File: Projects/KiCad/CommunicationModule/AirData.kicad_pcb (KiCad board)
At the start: 2 copper layers, 110 x 95 mm, 26 parts, among them J1 Conn_01x04_Pin, J2 Conn_01x04_Pin, J3 Micro_SD_Card_Det_Hirose_DM3AT, U1 ABX00012, U2 MCP2562-E-P, U3 LT1584-3.3, U4 TLP222A, U5 MCP2515-I/P, Y1 8MHz

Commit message: ミッションモジュール, エアデータ通信モジュール, システムデータ通信モジュールのKiCadを追加
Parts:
- removed C3, C4: 0.1μF, Capacitor_SMD:C_0805_2012Metric_Pad1.18x1.45mm_HandSolder
- removed D1: 1N4148, Diode_THT:D_DO-35_SOD27_P7.62mm_Horizontal
- removed F1: Polyfuse, Fuse:Fuse_BelFuse_0ZRE0005FF_L8.3mm_W3.8mm
- removed J3: Micro_SD_Card_Det_Hirose_DM3AT, Connector_Card:microSD_HC_Hirose_DM3AT-SF-PEJM5
- removed R3, R4: 120Ω, Resistor_SMD:R_0805_2012Metric_Pad1.20x1.40mm_HandSolder
- removed U3: LT1584-3.3, Package_TO_SOT_THT:TO-220-3_Vertical
- removed U4: TLP222A, Package_DIP:DIP-4_W7.62mm
- removed U6: ~, StrawberryLinux_ADXL375_Module:ADXL375
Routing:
- net +3.3V: track 159.2 -> 79.2 mm, vias 4 -> 2
- net I2C_SDA: track 57.8 -> 0.00 mm
- net I2C_SCL: track 55.3 -> 0.00 mm
- net SPI_MISO: track 75.9 -> 27.6 mm
- net SPI_SCLK: track 65.8 -> 21.2 mm
- net +5V: track 106.8 -> 65.6 mm, vias 3 -> 1
- net SPI_MOSI: track 61.8 -> 21.2 mm
- net Net-(D1-A): track 36.2 -> 0.00 mm, vias 1 -> 0
- net MEMORY_POWER_CONTROL: track 36.1 -> 0.00 mm, vias 1 -> 0
- net SPI_CS_SD: track 34.2 -> 0.00 mm
- net MEMORY_POWER: track 19.9 -> 0.00 mm
- net Net-(R3-Pad2): track 9.35 -> 0.00 mm
- net Net-(F1-Pad2): track 7.06 -> 0.00 mm

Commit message: 全モジュールのkicadを一通り作った
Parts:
- added D1: LED, LED_SMD:LED_1206_3216Metric_Pad1.42x1.75mm_HandSolder, F.Cu at (187.0, 73.5)
- added D2: LED, LED_SMD:LED_1206_3216Metric_Pad1.42x1.75mm_HandSolder, F.Cu at (195.5, 109.5)
- added D3: LED, LED_SMD:LED_1206_3216Metric_Pad1.42x1.75mm_HandSolder, F.Cu at (195.5, 114.5)
- added D4: LED, LED_SMD:LED_1206_3216Metric_Pad1.42x1.75mm_HandSolder, F.Cu at (158.5, 134.5)
- added D5: LED, LED_SMD:LED_1206_3216Metric_Pad1.42x1.75mm_HandSolder, F.Cu at (151.5, 134.5)
- added R2: 10kΩ, Resistor_SMD:R_0805_2012Metric_Pad1.20x1.40mm_HandSolder, F.Cu at (172.5, 119.0)
- added R3: 2kΩ, Resistor_SMD:R_0805_2012Metric_Pad1.20x1.40mm_HandSolder, F.Cu at (187.0, 77.0)
- added R4: 100Ω, Resistor_SMD:R_0805_2012Metric_Pad1.20x1.40mm_HandSolder, F.Cu at (190.5, 109.5)
- added R5: 100Ω, Resistor_SMD:R_0805_2012Metric_Pad1.20x1.40mm_HandSolder, F.Cu at (190.5, 114.5)
- added R6: 100Ω, Resistor_SMD:R_0805_2012Metric_Pad1.20x1.40mm_HandSolder, F.Cu at (158.5, 129.0)
- added R7: 100Ω, Resistor_SMD:R_0805_2012Metric_Pad1.20x1.40mm_HandSolder, F.Cu at (151.5, 129.0)
- added SW1: SW_Push, Button_Switch_THT:SW_PUSH_6mm, F.Cu at (141.8, 133.8)
- moved C3 0.71 mm to (172.5, 121.5), turned to 180 degrees
- renumbered C5 to C3, C6 to C4, C7 to C5, U5 to U3
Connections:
- U1 pad 10: unconnected-(U1-PA23_TC4-W1/1-Pad10) -> CAN_RECEIVE_STATUS
- U1 pad 11: unconnected-(U1-PA10_TCC0-W2/~2-Pad11) -> CAN_SEND_STATUS
- U1 pad 12: unconnected-(U1-PA11_TCC0-W3/~3-Pad12) -> LORA_RECEIVE_STATUS
- U1 pad 13: unconnected-(U1-PB10_TCC0-W4/~4-Pad13) -> LORA_SEND_STATUS
- U1 pad 14: MEMORY_POWER_CONTROL -> unconnected-(U1-PB11_TCC0-W5/~5-Pad14)
- U1 pad 15: SPI_CS_SD -> unconnected-(U1-PA20_TCC0-W6-Pad15)
- U1 pad 20: I2C_SDA -> unconnected-(U1-PA08_S0_I2C_SDA-Pad20)
- U1 pad 21: I2C_SCL -> unconnected-(U1-PA09_S0_I2C_SCL-Pad21)
- U1 pad 9: unconnected-(U1-PA22_TC4-W0/0-Pad9) -> DEBUG_MODE
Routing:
- net CAN_RECEIVE_STATUS: track 0.00 -> 76.9 mm
- net CAN_SEND_STATUS: track 0.00 -> 72.0 mm
- net DEBUG_MODE: track 0.00 -> 42.7 mm
- net LORA_RECEIVE_STATUS: track 0.00 -> 33.4 mm
- net LORA_SEND_STATUS: track 0.00 -> 28.9 mm
- net +5V: track 65.6 -> 70.1 mm
- net Net-(D1-A): track 0.00 -> 3.70 mm
- net Net-(U3-~RESET): track 0.00 -> 3.23 mm
- net Net-(D5-A): track 0.00 -> 3.01 mm
- net Net-(D4-A): track 0.00 -> 3.01 mm
- net Net-(D3-A): track 0.00 -> 2.51 mm
- net Net-(D2-A): track 0.00 -> 2.51 mm
- net CAN_TX: track 45.2 -> 46.1 mm
- net +3.3V: track 79.2 -> 79.7 mm
- net GND: vias 0 -> 58
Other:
- board text added: "Boot Selection"
- board text added: "CAN"
- board text added: "CAN-BUS TERMINATION RESISTOR (OPTIONAL)"
- board text added: "DEBUG"
- board text added: "LORA"
- board text added: "POWER"
- board text added: "RECEIVE"
- board text added: "SEND"

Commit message: 一通り部品を選定
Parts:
- C4, C5: footprint Capacitor_SMD:C_0805_2012Metric_Pad1.18x1.45mm_HandSolder -> Capacitor_SMD:C_0603_1608Metric_Pad1.08x0.95mm_HandSolder
- D1: value LED -> RED; footprint LED_SMD:LED_1206_3216Metric_Pad1.42x1.75mm_HandSolder -> LED_SMD:LED_0603_1608Metric_Pad1.05x0.95mm_HandSolder
- D2, D3, D4, D5: value LED -> ORANGE; footprint LED_SMD:LED_1206_3216Metric_Pad1.42x1.75mm_HandSolder -> LED_SMD:LED_0603_1608Metric_Pad1.05x0.95mm_HandSolder
- R1: value 120R1/4W -> 120Ω; footprint Resistor_SMD:R_0805_2012Metric_Pad1.20x1.40mm_HandSolder -> Resistor_SMD:R_0603_1608Metric_Pad0.98x0.95mm_HandSolder
- R2, R4, R5, R6, R7: footprint Resistor_SMD:R_0805_2012Metric_Pad1.20x1.40mm_HandSolder -> Resistor_SMD:R_0603_1608Metric_Pad0.98x0.95mm_HandSolder
- R3: value 2kΩ -> 620Ω; footprint Resistor_SMD:R_0805_2012Metric_Pad1.20x1.40mm_HandSolder -> Resistor_SMD:R_0603_1608Metric_Pad0.98x0.95mm_HandSolder
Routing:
- net Net-(D5-A): track 3.01 -> 3.62 mm
- net Net-(D4-A): track 3.01 -> 3.62 mm
- net Net-(D3-A): track 2.51 -> 3.12 mm
- net Net-(D2-A): track 2.51 -> 3.12 mm

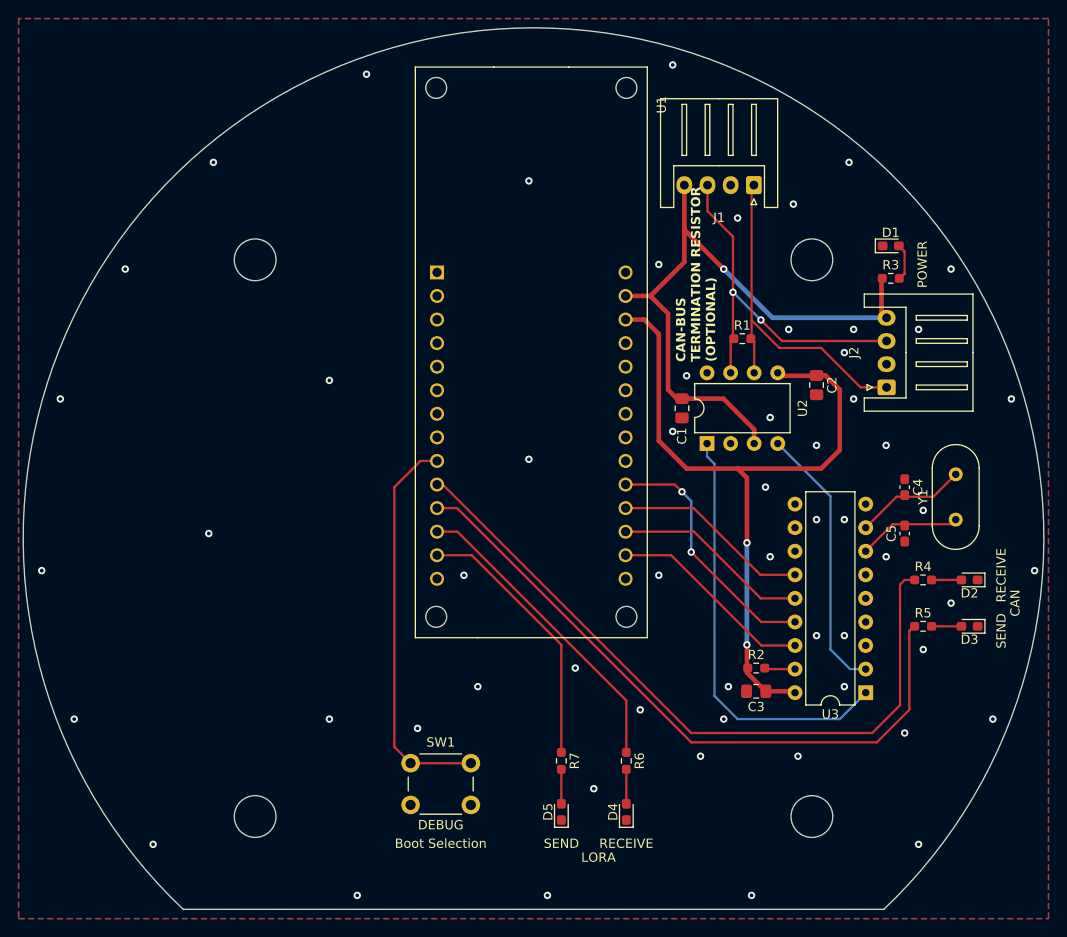
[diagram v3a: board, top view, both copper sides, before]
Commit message: コネクタを再配置, 基板上で12V->5Vをするように変更
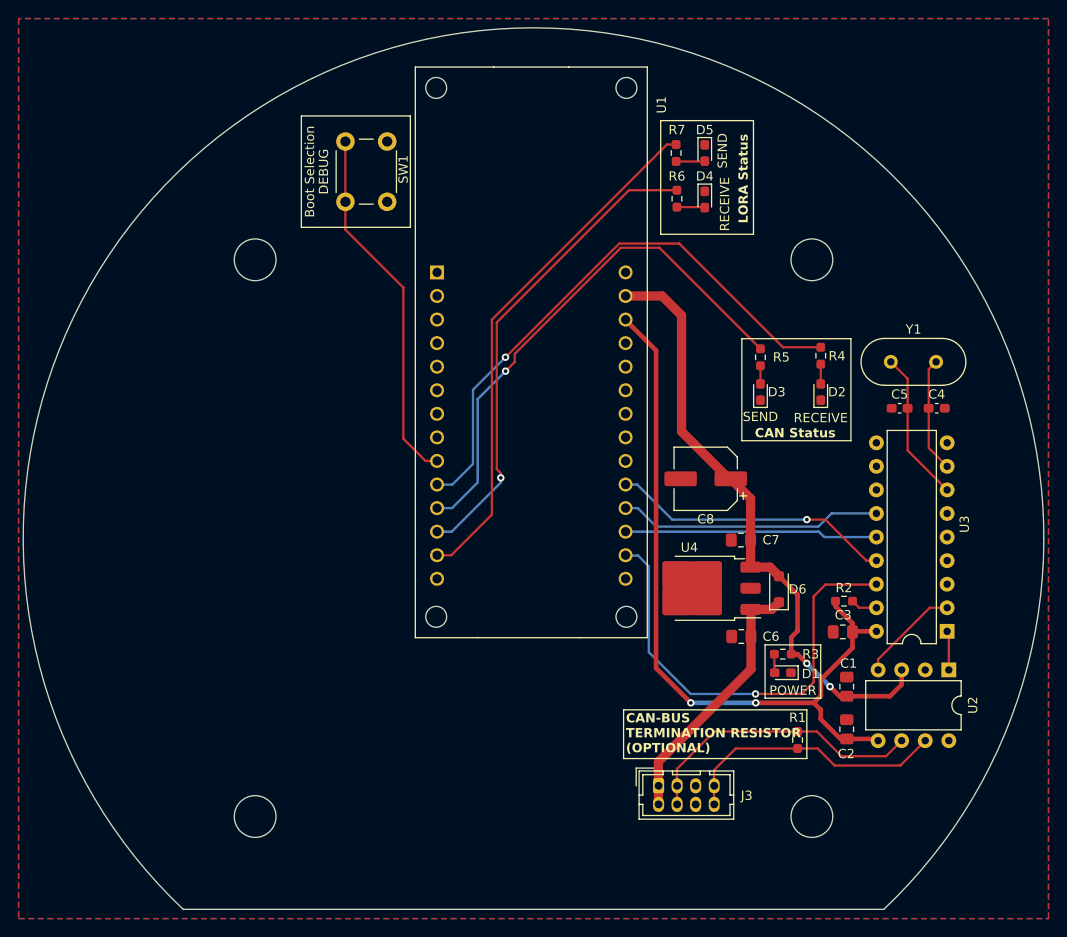
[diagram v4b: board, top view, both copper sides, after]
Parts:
- removed J1, J2: Conn_01x04_Pin, Connector_JST:JST_XH_S4B-XH-A_1x04_P2.50mm_Horizontal
- added C6: 0.33μF, Capacitor_SMD:C_0805_2012Metric_Pad1.18x1.45mm_HandSolder, F.Cu at (170.9, 115.6)
- added C7: 0.1μF, Capacitor_SMD:C_0805_2012Metric_Pad1.18x1.45mm_HandSolder, F.Cu at (170.9, 105.2)
- added C8: 100μF, Capacitor_SMD:CP_Elec_6.3x7.7, F.Cu at (167.1, 98.6)
- added D6: 1N4007, Diode_SMD:D_SOD-123F, F.Cu at (175.0, 110.5)
- added J3: Conn_01x08, Connector_Hirose:Hirose_DF11-8DP-2DSA_2x04_P2.00mm_Vertical, F.Cu at (162.0, 131.7)
- added U4: NJM7805SDL1, Package_TO_SOT_SMD:TO-252-3_TabPin2, F.Cu at (166.9, 110.4)
- moved D5 72.7 mm to (167.0, 63.5), turned to -90 degrees
- moved SW1 72.1 mm to (132.7, 62.2), turned to -90 degrees
- moved R7 66.7 mm to (163.9, 63.5)
- moved D4 66.5 mm to (167.0, 68.5), turned to -90 degrees
- moved R6 60.8 mm to (164.0, 68.4)
- moved D1 47.4 mm to (175.4, 119.5), turned to 180 degrees
- moved R1 43.7 mm to (177.0, 126.8), turned to 90 degrees
- moved R3 42.1 mm to (175.4, 117.5), turned to 180 degrees
- moved C2 37.2 mm to (182.3, 125.6), turned to 90 degrees
- moved U2 35.7 mm to (193.3, 119.2), turned to -90 degrees
- moved C1 34.9 mm to (182.3, 121.0), turned to 90 degrees
- moved R5 33.9 mm to (173.0, 85.5), turned to -90 degrees
- moved D3 33.8 mm to (173.0, 89.3), turned to 90 degrees
- moved R4 26.6 mm to (179.5, 85.3), turned to -90 degrees
- moved D2 25.8 mm to (179.5, 89.3), turned to 90 degrees
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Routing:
- net CAN_TX: track 46.1 -> 3.98 mm
- net +12V: track 0.00 -> 28.5 mm
- net LORA_SEND_STATUS: track 28.9 -> 56.4 mm
- net SPI_CS_MCP: track 22.3 -> 49.0 mm, vias 0 -> 1
- net LORA_RECEIVE_STATUS: track 33.4 -> 51.8 mm, vias 0 -> 1
- net CAN_RX: track 29.2 -> 10.9 mm
- net CAN_RECEIVE_STATUS: track 76.9 -> 61.4 mm, vias 0 -> 1
- net CAN_SEND_STATUS: track 72.0 -> 56.8 mm, vias 0 -> 1
- net CAN_H: track 40.2 -> 29.3 mm, vias 2 -> 0
- net SPI_SCLK: track 21.2 -> 28.5 mm
- net CAN_L: track 38.0 -> 31.5 mm
- net SPI_MOSI: track 21.2 -> 27.3 mm
- net OSC2: track 11.1 -> 16.3 mm
- net +5V: track 70.1 -> 65.9 mm, vias 1 -> 2
- net DEBUG_MODE: track 42.7 -> 39.2 mm
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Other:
- board text added: "CAN Status"
- board text added: "LORA Status"
- board text removed: "CAN"
- board text removed: "LORA"

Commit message: 基板設計の都市伝説をいろいろ適応
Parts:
- REF** (x4): value MountingHole_4.5mm -> MountingHole_4.5mm_Pad_Via; footprint MountingHole:MountingHole_4.5mm -> MountingHole:MountingHole_4.5mm_Pad_Via
- moved R1 17.1 mm to (193.9, 129.0), turned to 0 degrees
- renumbered C4 to C1, C6 to C2, C2 to C3, C1 to C4, C3 to C5, C7 to C6, C5 to C7, D3 to D2, D2 to D3, D6 to D4, D4 to D5, D5 to D6, J3 to J1, R3 to R2, R2 to R3, U2 to U1, U3 to U2, U4 to U3, U1 to U4
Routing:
- net CAN_L: track 31.5 -> 43.7 mm
- net CAN_H: track 29.3 -> 40.0 mm
- net +3.3V: track 82.4 -> 85.5 mm, vias 2 -> 4
- net +5V: track 65.9 -> 67.7 mm, vias 2 -> 4
- net GND: vias 0 -> 147
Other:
- board text added: "CAN-BUS Termination Resistor"
- board text removed: "CAN-BUS TERMINATION RESISTOR (OPTIONAL)"

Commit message: 裏面にQRコードと署名を追加
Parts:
- added G***: LOGO, LOGO, B.Cu at (148.0, 63.5)
- added G***: LOGO, LOGO, B.Cu at (146.5, 74.5)
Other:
- board text added: "Communication Module Air Data Build 1"
- board text added: "Designed by Y.Iwai 2023"
- board text added: "Tokai Student Rocket Poject H-58 Avionics"

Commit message: コネクタ類の3Dモデルを追加
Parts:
- J1: footprint Connector_Hirose:Hirose_DF11-8DP-2DSA_2x04_P2.00mm_Vertical -> Hirose_Connector:Hirose_DF11B-8DP-2DS
